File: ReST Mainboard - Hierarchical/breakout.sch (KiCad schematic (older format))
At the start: 11 parts, among them P16 CONN_02X05, P17 CONN_02X05, P18 CONN_02X05, P19 CONN_01X04, P20 CONN_01X02, P21 CONN_01X04, P22 CONN_02X03, P23 CONN_02X03, P24 CONN_01X04, P25 CONN_02X03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

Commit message: started routing
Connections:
- net +3V3: now also P26.1 (P1), P26.3 (P3), P26.5 (P5); no longer P26.2 (P2), P26.4 (P4), P26.6 (P6)
- net +5V: now also P26.2 (P2), P26.4 (P4), P26.6 (P6); no longer P26.1 (P1), P26.3 (P3), P26.5 (P5)
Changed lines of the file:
@@
 F 3 "" H 6450 1650 50  0000 C CNN
 	1    6450 2850
-	1    0    0    -1
+	-1   0    0    -1
 $EndComp
 $Comp

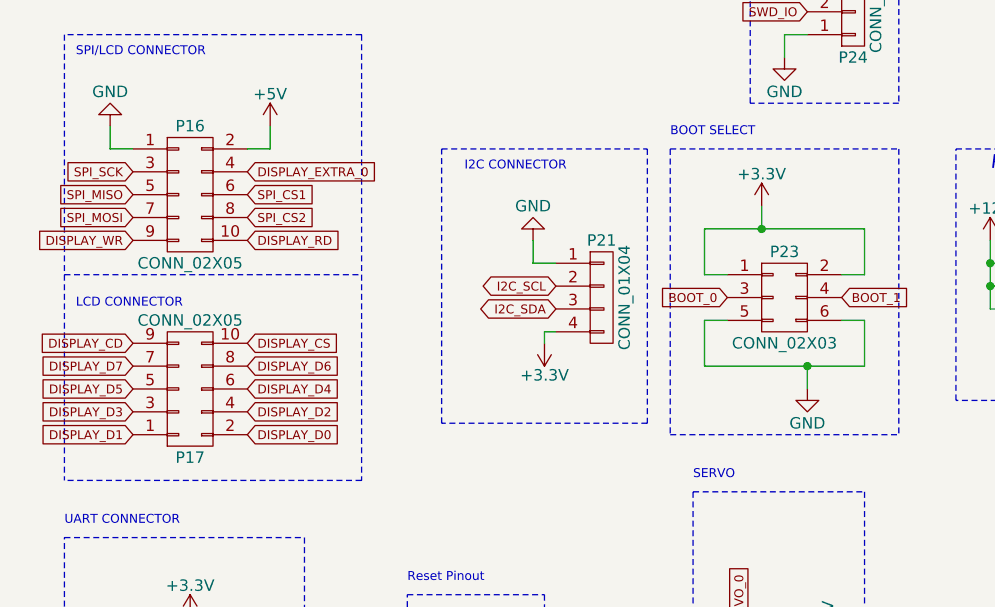
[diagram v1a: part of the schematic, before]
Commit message: Mostly finished with main PCB. Only need to work the High Current Stuff out. On Vacation for now
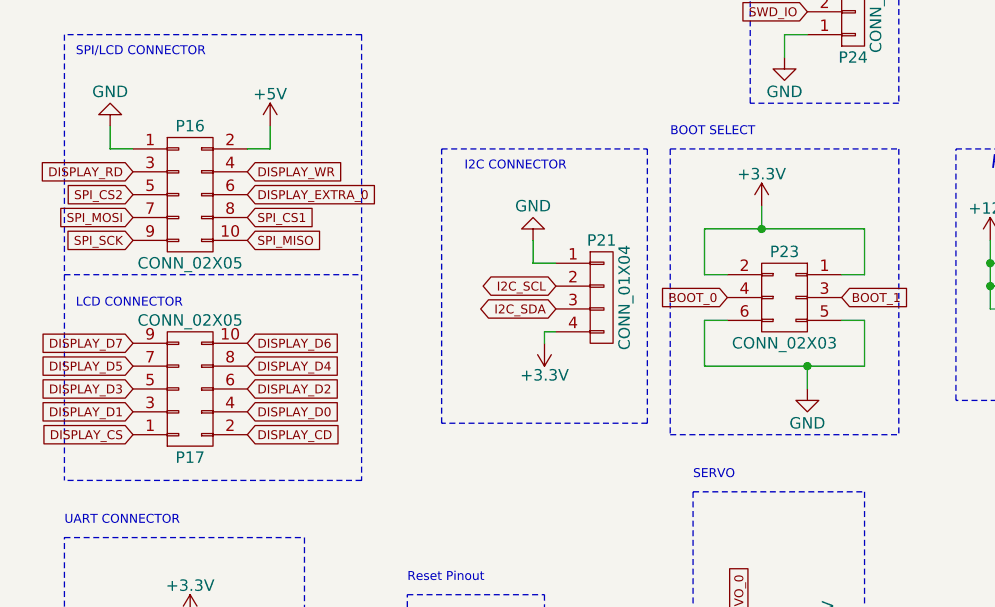
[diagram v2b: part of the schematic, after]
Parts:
- P19, P24: footprint Pin_Headers:Pin_Header_Straight_1x04 -> ReST-Library:bb02-hy04a
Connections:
- net BOOT_0: now also P23.4 (P4); no longer P23.3 (P3)
- net BOOT_1: now also P23.3 (P3); no longer P23.4 (P4)
- net DISPLAY_CD: now also P17.2 (P2); no longer P17.9 (P9)
- net DISPLAY_CS: now also P17.1 (P1); no longer P17.10 (P10)
- net DISPLAY_D0: now also P17.4 (P4); no longer P17.2 (P2)
- net DISPLAY_D1: now also P17.3 (P3); no longer P17.1 (P1)
- net DISPLAY_D2: now also P17.6 (P6); no longer P17.4 (P4)
- net DISPLAY_D3: now also P17.5 (P5); no longer P17.3 (P3)
- net DISPLAY_D4: now also P17.8 (P8); no longer P17.6 (P6)
- net DISPLAY_D5: now also P17.7 (P7); no longer P17.5 (P5)
- net DISPLAY_D6: now also P17.10 (P10); no longer P17.8 (P8)
- net DISPLAY_D7: now also P17.9 (P9); no longer P17.7 (P7)
- net DISPLAY_EXTRA_0: now also P16.6 (P6); no longer P16.4 (P4)
- net DISPLAY_RD: now also P16.3 (P3); no longer P16.10 (P10)
- net DISPLAY_WR: now also P16.4 (P4); no longer P16.9 (P9)
- net SPI_CS1: now also P16.8 (P8); no longer P16.6 (P6)
- net SPI_CS2: now also P16.5 (P5); no longer P16.8 (P8)
- net SPI_MISO: now also P16.10 (P10); no longer P16.5 (P5)
- net SPI_SCK: now also P16.9 (P9); no longer P16.3 (P3)
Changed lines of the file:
@@
 $EndDescr
 $Comp
-L GND #PWR0133
+L GND #PWR0134
 U 1 1 57792A39
 P 5900 3150
-F 0 "#PWR0133" H 5900 2900 50  0001 C CNN
+F 0 "#PWR0134" H 5900 2900 50  0001 C CNN
 F 1 "GND" H 5900 3000 50  0000 C CNN
 F 2 "" H 5900 3150 50  0000 C CNN
@@
 $EndComp
 $Comp
-L +12V #PWR0134
+L +12V #PWR0135
 U 1 1 57792A3F
 P 5200 2650
-F 0 "#PWR0134" H 5200 2500 50  0001 C CNN
+F 0 "#PWR0135" H 5200 2500 50  0001 C CNN
 F 1 "+12V" H 5200 2790 50  0000 C CNN
 F 2 "" H 5200 2650 50  0000 C CNN
@@
 $EndComp
 $Comp
-L +5V #PWR0135
+L +5V #PWR0136
 U 1 1 57792A45
 P 6100 2650
-F 0 "#PWR0135" H 6100 2500 50  0001 C CNN
+F 0 "#PWR0136" H 6100 2500 50  0001 C CNN
 F 1 "+5V" H 6100 2790 50  0000 C CNN
 F 2 "" H 6100 2650 50  0000 C CNN
@@
 $EndComp
 $Comp
-L +3.3V #PWR0136
+L +3.3V #PWR0137
 U 1 1 57792A4B
 P 6800 2650
-F 0 "#PWR0136" H 6800 2500 50  0001 C CNN
+F 0 "#PWR0137" H 6800 2500 50  0001 C CNN
 F 1 "+3.3V" H 6800 2790 50  0000 C CNN
 F 2 "" H 6800 2650 50  0000 C CNN
@@
 	6800 2650 6800 2950
 $Comp
-L +3.3V #PWR0137
+L +3.3V #PWR0138
 U 1 1 5779318E
 P 4200 2500
-F 0 "#PWR0137" H 4200 2350 50  0001 C CNN
+F 0 "#PWR0138" H 4200 2350 50  0001 C CNN
 F 1 "+3.3V" H 4200 2640 50  0000 C CNN
 F 2 "" H 4200 2500 50  0000 C CNN
@@
 $EndComp
 $Comp
-L GND #PWR0138
+L GND #PWR0139
 U 1 1 57793194
 P 1350 2150
-F 0 "#PWR0138" H 1350 1900 50  0001 C CNN
+F 0 "#PWR0139" H 1350 1900 50  0001 C CNN
 F 1 "GND" H 1350 2000 50  0000 C CNN
 F 2 "" H 1350 2150 50  0000 C CNN
@@
 $EndComp
 $Comp
-L +5V #PWR0139
+L +5V #PWR0140
 U 1 1 5779319A
 P 2050 2150
-F 0 "#PWR0139" H 2050 2000 50  0001 C CNN
+F 0 "#PWR0140" H 2050 2000 50  0001 C CNN
 F 1 "+5V" H 2050 2290 50  0000 C CNN
 F 2 "" H 2050 2150 50  0000 C CNN
@@
 BOOT SELECT
 $Comp
-L GND #PWR0140
+L GND #PWR0141
 U 1 1 577931A7
 P 3200 2650
-F 0 "#PWR0140" H 3200 2400 50  0001 C CNN
+F 0 "#PWR0141" H 3200 2400 50  0001 C CNN
 F 1 "GND" H 3200 2500 50  0000 C CNN
 F 2 "" H 3200 2650 50  0000 C CNN
@@
 $EndComp
 $Comp
-L GND #PWR0141
+L GND #PWR0142
 U 1 1 577931B9
 P 4300 1850
-F 0 "#PWR0141" H 4300 1600 50  0001 C CNN
+F 0 "#PWR0142" H 4300 1600 50  0001 C CNN
 F 1 "GND" H 4300 1700 50  0000 C CNN
 F 2 "" H 4300 1850 50  0000 C CNN
@@
 F 3 "" H 4300 1700 50  0000 C CNN
 	1    4300 2900
-	1    0    0    -1
-$EndComp
-$Comp
-L GND #PWR0142
+	-1   0    0    -1
+$EndComp
+$Comp
+L GND #PWR0143
 U 1 1 577931E4
 P 4400 3300
-F 0 "#PWR0142" H 4400 3050 50  0001 C CNN
+F 0 "#PWR0143" H 4400 3050 50  0001 C CNN
 F 1 "GND" H 4400 3150 50  0000 C CNN
 F 2 "" H 4400 3300 50  0000 C CNN
@@
 $EndComp
 $Comp
-L GND #PWR0143
+L GND #PWR0144
 U 1 1 577931F1
 P 4400 5000
-F 0 "#PWR0143" H 4400 4750 50  0001 C CNN
+F 0 "#PWR0144" H 4400 4750 50  0001 C CNN
 F 1 "GND" H 4400 4850 50  0000 C CNN
 F 2 "" H 4400 5000 50  0000 C CNN
@@
 $EndComp
 $Comp
-L +5V #PWR0144
+L +5V #PWR0145
 U 1 1 577931F7
 P 4350 4300
-F 0 "#PWR0144" H 4350 4150 50  0001 C CNN
+F 0 "#PWR0145" H 4350 4150 50  0001 C CNN
 F 1 "+5V" H 4350 4440 50  0000 C CNN
 F 2 "" H 4350 4300 50  0000 C CNN
@@
 F 0 "P19" H 2000 4800 50  0000 C CNN
 F 1 "CONN_01X04" V 2100 4550 50  0000 C CNN
-F 2 "Pin_Headers:Pin_Header_Straight_1x04" H 2000 4550 50  0001 C CNN
+F 2 "ReST-Library:bb02-hy04a" H 2000 4550 50  0001 C CNN
 F 3 "" H 2000 4550 50  0000 C CNN
 	1    2000 4550
@@
 $EndComp
 $Comp
-L GND #PWR0145
+L GND #PWR0146
 U 1 1 57793206
 P 1700 4800
-F 0 "#PWR0145" H 1700 4550 50  0001 C CNN
+F 0 "#PWR0146" H 1700 4550 50  0001 C CNN
 F 1 "GND" H 1700 4650 50  0000 C CNN
 F 2 "" H 1700 4800 50  0000 C CNN
@@
 F 0 "P24" H 4600 1850 50  0000 C CNN
 F 1 "CONN_01X04" V 4700 1600 50  0000 C CNN
-F 2 "Pin_Headers:Pin_Header_Straight_1x04" H 4600 1600 50  0001 C CNN
+F 2 "ReST-Library:bb02-hy04a" H 4600 1600 50  0001 C CNN
 F 3 "" H 4600 1600 50  0000 C CNN
 	1    4600 1600
@@
 Extra Pinout
 $Comp
-L GND #PWR0146
+L GND #PWR0147
 U 1 1 57793214
 P 1850 5900
-F 0 "#PWR0146" H 1850 5650 50  0001 C CNN
+F 0 "#PWR0147" H 1850 5650 50  0001 C CNN
 F 1 "GND" H 1850 5750 50  0000 C CNN
 F 2 "" H 1850 5900 50  0000 C CNN
@@
 $EndComp
 $Comp
-L +3.3V #PWR0147
+L +3.3V #PWR0148
 U 1 1 5779321A
 P 3250 3100
-F 0 "#PWR0147" H 3250 2950 50  0001 C CNN
+F 0 "#PWR0148" H 3250 2950 50  0001 C CNN
 F 1 "+3.3V" H 3250 3240 50  0000 C CNN
 F 2 "" H 3250 3100 50  0000 C CNN
@@
 $EndComp
 $Comp
-L +3.3V #PWR0148
+L +3.3V #PWR0149
 U 1 1 57793220
 P 4300 1350
-F 0 "#PWR0148" H 4300 1200 50  0001 C CNN
+F 0 "#PWR0149" H 4300 1200 50  0001 C CNN
 F 1 "+3.3V" H 4300 1490 50  0000 C CNN
 F 2 "" H 4300 1350 50  0000 C CNN
@@
 $EndComp
 $Comp
-L +3.3V #PWR0149
+L +3.3V #PWR0150
 U 1 1 57793226
 P 1700 4300
-F 0 "#PWR0149" H 1700 4150 50  0001 C CNN
+F 0 "#PWR0150" H 1700 4150 50  0001 C CNN
 F 1 "+3.3V" H 1700 4440 50  0000 C CNN
 F 2 "" H 1700 4300 50  0000 C CNN
@@
 $EndComp
 $Comp
-L GND #PWR0150
+L GND #PWR0151
 U 1 1 57793233
 P 2850 4600
-F 0 "#PWR0150" H 2850 4350 50  0001 C CNN
+F 0 "#PWR0151" H 2850 4350 50  0001 C CNN
 F 1 "GND" H 2850 4450 50  0000 C CNN
 F 2 "" H 2850 4600 50  0000 C CNN
@@
 	3250 4800 2650 4800
 Wire Notes Line
-	3250 4200 3250 4800
-Wire Notes Line
 	2650 4200 3250 4200
 Wire Notes Line
@@
 Text GLabel 1450 2550 0    39   Input ~ 0
 SPI_MOSI
-Text GLabel 1450 2450 0    39   Input ~ 0
+Text GLabel 1950 2650 2    39   Input ~ 0
 SPI_MISO
-Text GLabel 1450 2350 0    39   Input ~ 0
+Text GLabel 1450 2650 0    39   Input ~ 0
 SPI_SCK
-Text GLabel 1450 3100 0    39   Input ~ 0
+Text GLabel 1950 3500 2    39   Input ~ 0
 DISPLAY_CD
 Text GLabel 4400 1550 0    39   Input ~ 0
@@
 Text GLabel 3300 2950 0    39   BiDi ~ 0
 I2C_SDA
+Text GLabel 1950 2450 2    39   Input ~ 0
+DISPLAY_EXTRA_0
+Text GLabel 1450 2350 0    39   Input ~ 0
+DISPLAY_RD
 Text GLabel 1950 2350 2    39   Input ~ 0
-DISPLAY_EXTRA_0
-Text GLabel 1950 2650 2    39   Input ~ 0
-DISPLAY_RD
-Text GLabel 1450 2650 0    39   Input ~ 0
 DISPLAY_WR
+Text GLabel 1450 2450 0    39   Input ~ 0
+SPI_CS2
 Text GLabel 1950 2550 2    39   Input ~ 0
-SPI_CS2
-Text GLabel 1950 2450 2    39   Input ~ 0
 SPI_CS1
-Text GLabel 1950 3100 2    39   Input ~ 0
+Text GLabel 1450 3500 0    39   Input ~ 0
 DISPLAY_CS
 Text GLabel 4100 4400 1    39   Input ~ 0
 SERVO_0
-Text GLabel 1950 3500 2    39   Input ~ 0
+Text GLabel 1950 3400 2    39   Input ~ 0
 DISPLAY_D0
-Text GLabel 1450 3500 0    39   Input ~ 0
+Text GLabel 1450 3400 0    39   Input ~ 0
 DISPLAY_D1
-Text GLabel 1950 3400 2    39   Input ~ 0
+Text GLabel 1950 3300 2    39   Input ~ 0
 DISPLAY_D2
-Text GLabel 1450 3400 0    39   Input ~ 0
+Text GLabel 1450 3300 0    39   Input ~ 0
 DISPLAY_D3
-Text GLabel 1950 3300 2    39   Input ~ 0
+Text GLabel 1950 3200 2    39   Input ~ 0
 DISPLAY_D4
-Text GLabel 1450 3300 0    39   Input ~ 0
+Text GLabel 1450 3200 0    39   Input ~ 0
 DISPLAY_D5
-Text GLabel 1950 3200 2    39   Input ~ 0
+Text GLabel 1950 3100 2    39   Input ~ 0
 DISPLAY_D6
-Text GLabel 1450 3200 0    39   Input ~ 0
+Text GLabel 1450 3100 0    39   Input ~ 0
 DISPLAY_D7
 Text GLabel 2100 5400 2    39   Input ~ 0
@@
 Text GLabel 1800 4600 0    39   Input ~ 0
 UART_1_RX
+Wire Notes Line
+	3250 4200 3250 4800
 $EndSCHEMATC
